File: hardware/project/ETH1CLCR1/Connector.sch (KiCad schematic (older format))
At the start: 1 part, among them J1101 C64AC

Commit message: Schematic design
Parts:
- added C1621, C1622, C1623, C1624, C1625, C1626: 10p, Capacitor_SMD:C_0603_1608Metric_Pad1.05x0.95mm_HandSolder, symbol Device:C
- added K1001, K1002, K1003, K1004, K1005, K1006: HE3621A0510, symbol ETH1CLCR1:HE3621A0510
- added Q1605, Q1606, Q1607, Q1608, Q1609, Q1610: BC847W, Package_TO_SOT_SMD:SOT-323_SC-70, symbol Transistor_BJT:BC847W
- added R1621, R1622, R1623, R1624, R1625, R1626: 10k, Resistor_SMD:R_0603_1608Metric_Pad1.05x0.95mm_HandSolder, symbol Device:R
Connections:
- net A: now also K1001.4
- net B: now also K1002.4
- net C: now also K1003.4
- net D: now also K1004.4
- net E: now also K1005.4
- net F: now also K1006.4
- new net: K1001.3, Q1605.3 (C)
- new net: K1002.3, Q1606.3 (C)
- new net: K1003.3, Q1607.3 (C)
- new net: K1004.3, Q1608.3 (C)
- new net: K1005.3, Q1609.3 (C)
- new net: K1006.3, Q1610.3 (C)
- new net: C1621.1, Q1605.1 (B), R1621.2
- new net: C1622.1, Q1606.1 (B), R1622.2
- new net: C1623.1, Q1607.1 (B), R1623.2
- new net: C1624.1, Q1608.1 (B), R1624.2
- new net: C1625.1, Q1609.1 (B), R1625.2
- new net: C1626.1, Q1610.1 (B), R1626.2
- new net +5VF: K1001.2, K1002.2, K1003.2, K1004.2, K1005.2, K1006.2
- new net AGNDF: C1621.2, C1622.2, C1623.2, C1624.2, C1625.2, C1626.2, K1004.1, Q1605.2 (E), Q1606.2 (E), Q1607.2 (E), Q1608.2 (E), Q1609.2 (E), Q1610.2 (E)
- new net CXN_RELA: R1621.1
- new net CXN_RELB: R1622.1
- new net CXN_RELC: R1623.1
- new net CXN_RELD: R1624.1
- new net CXN_RELE: R1625.1
- new net CXN_RELF: R1626.1
- new net GUARD: K1003.1
- new net HCUR: K1001.1
- new net HPOT: K1006.1
- new net LCUR: K1002.1
- new net LPOT: K1005.1

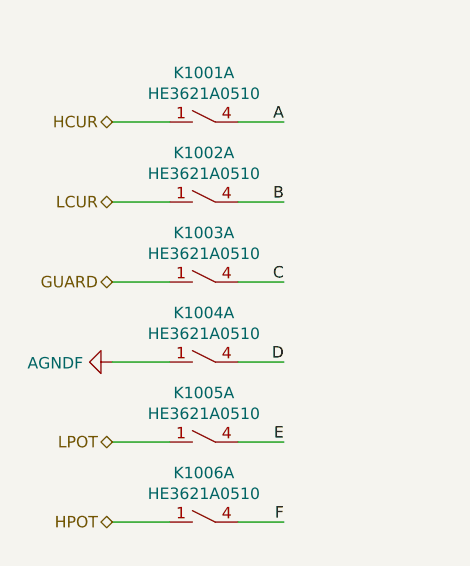
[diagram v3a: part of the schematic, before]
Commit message: Need to redesign the AC source, the LT1468 is too slow.
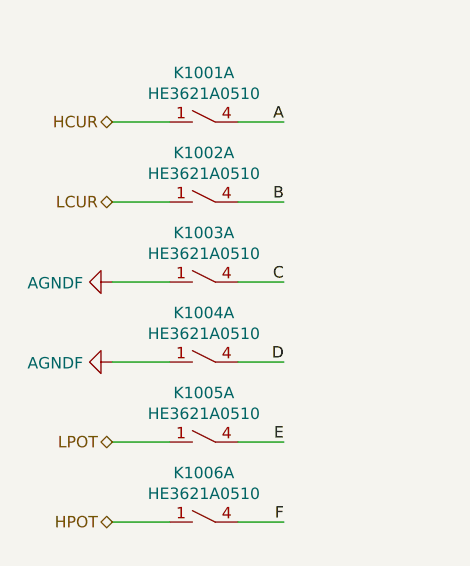
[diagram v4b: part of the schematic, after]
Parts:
- K1001, K1002, K1003, K1004, K1005, K1006: footprint (none) -> ETH1CLCR1:HE360_x-5050462-8
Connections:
- net GUARD is gone; now on net AGNDF: K1003.1
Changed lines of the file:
@@
 F 0 "K1001" V 3865 1300 50  0000 C CNN
 F 1 "HE3621A0510" V 3774 1300 50  0000 C CNN
-F 2 "" H 3900 1250 50  0001 C CNN
+F 2 "ETH1CLCR1:HE360_x-5050462-8" H 3900 1250 50  0001 C CNN
 F 3 "" H 3900 1250 50  0001 C CNN
 	1    3650 1300
@@
 F 0 "K1001" H 7978 1946 50  0000 L CNN
 F 1 "HE3621A0510" H 7978 1855 50  0000 L CNN
-F 2 "" H 8150 1850 50  0001 C CNN
+F 2 "ETH1CLCR1:HE360_x-5050462-8" H 8150 1850 50  0001 C CNN
 F 3 "" H 8150 1850 50  0001 C CNN
 	2    7900 1900
@@
 F 0 "K1002" V 3865 1650 50  0000 C CNN
 F 1 "HE3621A0510" V 3774 1650 50  0000 C CNN
-F 2 "" H 3900 1600 50  0001 C CNN
+F 2 "ETH1CLCR1:HE360_x-5050462-8" H 3900 1600 50  0001 C CNN
 F 3 "" H 3900 1600 50  0001 C CNN
 	1    3650 1650
@@
 F 0 "K1002" H 9728 1946 50  0000 L CNN
 F 1 "HE3621A0510" H 9728 1855 50  0000 L CNN
-F 2 "" H 9900 1850 50  0001 C CNN
+F 2 "ETH1CLCR1:HE360_x-5050462-8" H 9900 1850 50  0001 C CNN
 F 3 "" H 9900 1850 50  0001 C CNN
 	2    9650 1900
@@
 F 0 "K1003" V 3865 2000 50  0000 C CNN
 F 1 "HE3621A0510" V 3774 2000 50  0000 C CNN
-F 2 "" H 3900 1950 50  0001 C CNN
+F 2 "ETH1CLCR1:HE360_x-5050462-8" H 3900 1950 50  0001 C CNN
 F 3 "" H 3900 1950 50  0001 C CNN
 	1    3650 2000
@@
 F 0 "K1003" H 7978 3446 50  0000 L CNN
 F 1 "HE3621A0510" H 7978 3355 50  0000 L CNN
-F 2 "" H 8150 3350 50  0001 C CNN
+F 2 "ETH1CLCR1:HE360_x-5050462-8" H 8150 3350 50  0001 C CNN
 F 3 "" H 8150 3350 50  0001 C CNN
 	2    7900 3400
@@
 F 0 "K1004" V 3865 2350 50  0000 C CNN
 F 1 "HE3621A0510" V 3774 2350 50  0000 C CNN
-F 2 "" H 3900 2300 50  0001 C CNN
+F 2 "ETH1CLCR1:HE360_x-5050462-8" H 3900 2300 50  0001 C CNN
 F 3 "" H 3900 2300 50  0001 C CNN
 	1    3650 2350
@@
 F 0 "K1004" H 9728 3446 50  0000 L CNN
 F 1 "HE3621A0510" H 9728 3355 50  0000 L CNN
-F 2 "" H 9900 3350 50  0001 C CNN
+F 2 "ETH1CLCR1:HE360_x-5050462-8" H 9900 3350 50  0001 C CNN
 F 3 "" H 9900 3350 50  0001 C CNN
 	2    9650 3400
@@
 F 0 "K1005" V 3865 2700 50  0000 C CNN
 F 1 "HE3621A0510" V 3774 2700 50  0000 C CNN
-F 2 "" H 3900 2650 50  0001 C CNN
+F 2 "ETH1CLCR1:HE360_x-5050462-8" H 3900 2650 50  0001 C CNN
 F 3 "" H 3900 2650 50  0001 C CNN
 	1    3650 2700
@@
 F 0 "K1005" H 7978 4996 50  0000 L CNN
 F 1 "HE3621A0510" H 7978 4905 50  0000 L CNN
-F 2 "" H 8150 4900 50  0001 C CNN
+F 2 "ETH1CLCR1:HE360_x-5050462-8" H 8150 4900 50  0001 C CNN
 F 3 "" H 8150 4900 50  0001 C CNN
 	2    7900 4950
@@
 F 0 "K1006" V 3865 3050 50  0000 C CNN
 F 1 "HE3621A0510" V 3774 3050 50  0000 C CNN
-F 2 "" H 3900 3000 50  0001 C CNN
+F 2 "ETH1CLCR1:HE360_x-5050462-8" H 3900 3000 50  0001 C CNN
 F 3 "" H 3900 3000 50  0001 C CNN
 	1    3650 3050
@@
 F 0 "K1006" H 9728 4996 50  0000 L CNN
 F 1 "HE3621A0510" H 9728 4905 50  0000 L CNN
-F 2 "" H 9900 4900 50  0001 C CNN
+F 2 "ETH1CLCR1:HE360_x-5050462-8" H 9900 4900 50  0001 C CNN
 F 3 "" H 9900 4900 50  0001 C CNN
 	2    9650 4950
@@
 Text HLabel 3250 2700 0    50   BiDi ~ 0
 LPOT
-Text HLabel 3250 2000 0    50   BiDi ~ 0
-GUARD
 $Comp
 L Transistor_BJT:BC847W Q1605
@@
 	0    1    1    0
 $EndComp
+$Comp
+L ETH1CLCR1:AGNDF #PWR01650
+U 1 1 5E2C2319
+P 3250 2000
+F 0 "#PWR01650" H 3250 1750 50  0001 C CNN
+F 1 "AGNDF" V 3255 1872 50  0000 R CNN
+F 2 "" H 3250 2000 50  0001 C CNN
+F 3 "" H 3250 2000 50  0001 C CNN
+	1    3250 2000
+	0    1    1    0
+$EndComp

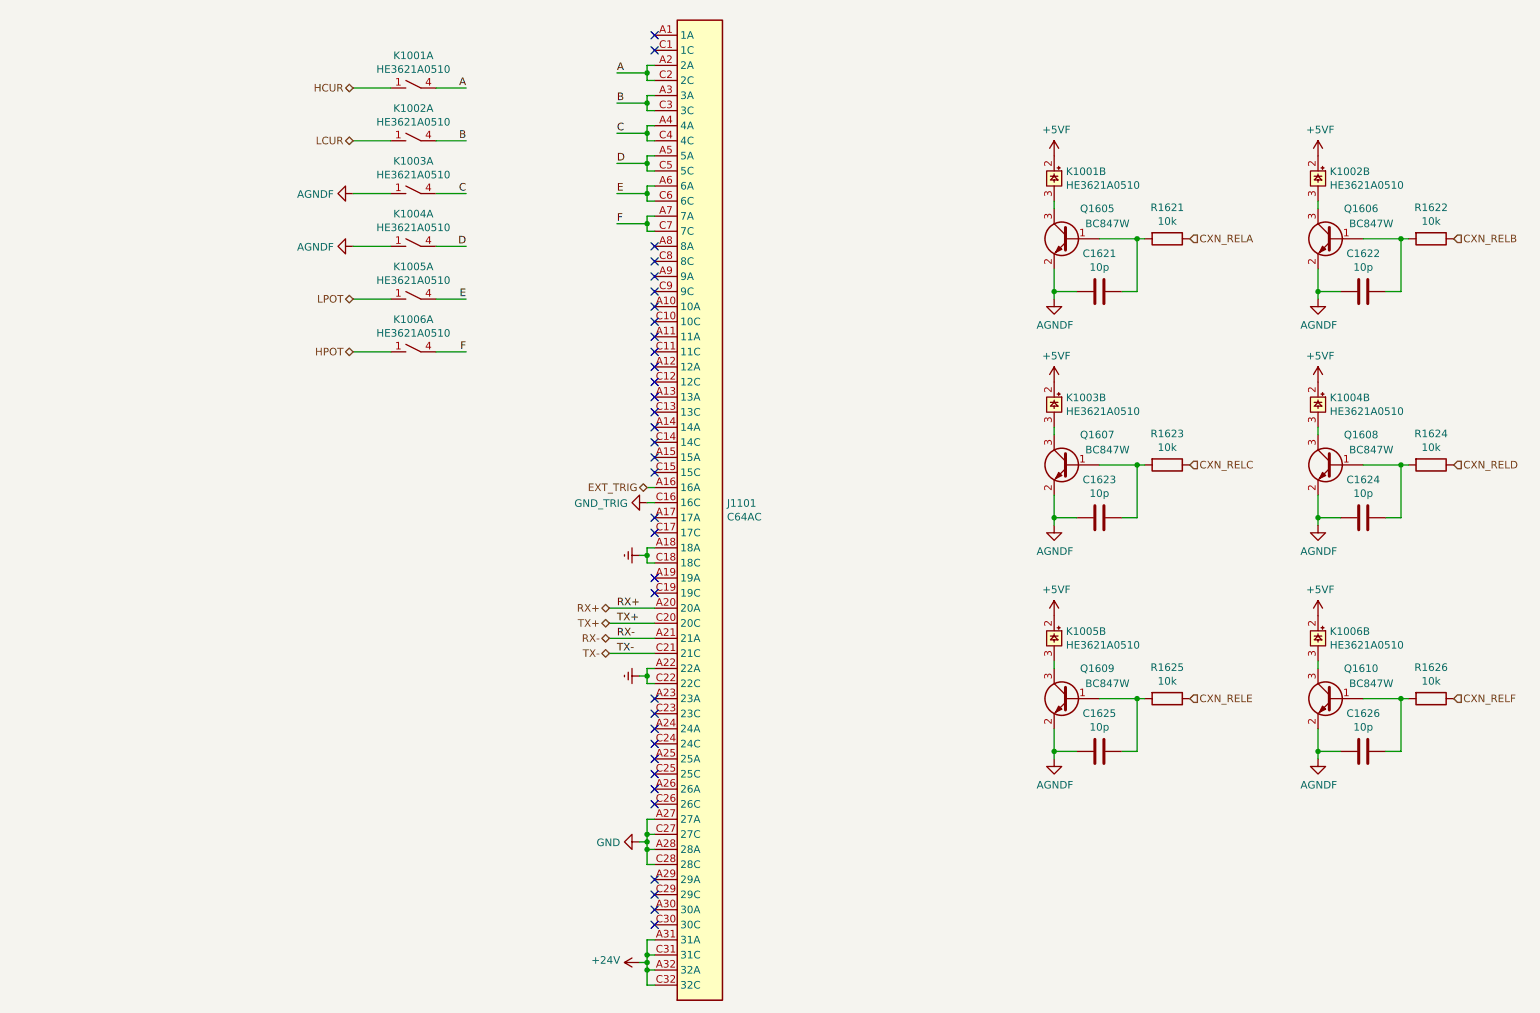
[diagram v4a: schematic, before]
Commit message: Footprint asigment (not finished).
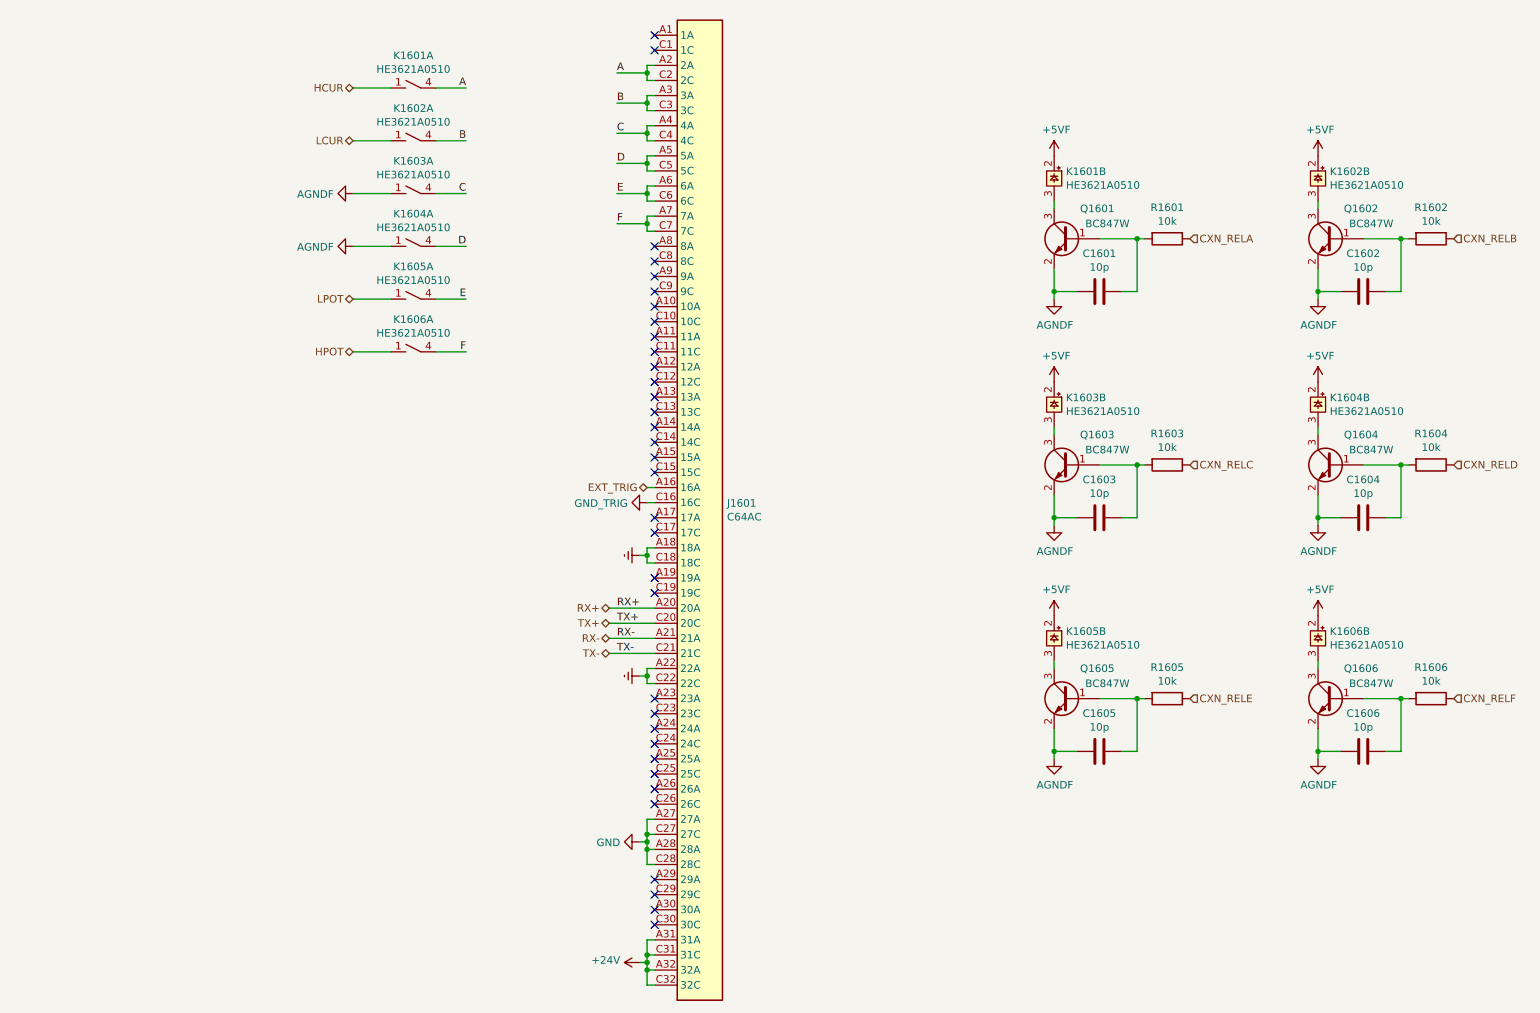
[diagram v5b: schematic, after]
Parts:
- renumbered C1621 to C1601, C1622 to C1602, C1623 to C1603, C1624 to C1604, C1625 to C1605, C1626 to C1606, J1101 to J1601, K1001 to K1601, K1002 to K1602, K1003 to K1603, K1004 to K1604, K1005 to K1605, K1006 to K1606, Q1605 to Q1601, Q1606 to Q1602, Q1607 to Q1603, Q1608 to Q1604, Q1609 to Q1605, Q1610 to Q1606, R1621 to R1601, R1622 to R1602, R1623 to R1603, R1624 to R1604, R1625 to R1605, R1626 to R1606

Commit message: Modification in schematic and PCB layout.
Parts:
- removed C1601, C1602, C1603, C1604, C1605, C1606: 10p, Capacitor_SMD:C_0603_1608Metric_Pad1.05x0.95mm_HandSolder, symbol Device:C
- removed Q1601, Q1602, Q1603, Q1604, Q1605, Q1606: BC847W, Package_TO_SOT_SMD:SOT-323_SC-70, symbol Transistor_BJT:BC847W
- removed R1601, R1602, R1603, R1604, R1605, R1606: 10k, Resistor_SMD:R_0603_1608Metric_Pad1.05x0.95mm_HandSolder, symbol Device:R
- added U1601: ULN2003A, Package_SO:TSSOP-16_4.4x5mm_P0.65mm, symbol Transistor_Array:ULN2003A
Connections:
- net +5VF: now also U1601.9 (COM)
- net AGNDF: now also U1601.8 (GND)
- net at K1601.3: now also U1601.16 (O1)
- net at K1602.3: now also U1601.15 (O2)
- net at K1603.3: now also U1601.14 (O3)
- net at K1604.3: now also U1601.13 (O4)
- net at K1605.3: now also U1601.12 (O5)
- net at K1606.3: now also U1601.11 (O6)
- new net CXN_REL1: U1601.1 (I1)
- new net CXN_REL2: U1601.2 (I2)
- new net CXN_REL3: U1601.3 (I3)
- new net CXN_REL4: U1601.4 (I4)
- new net CXN_REL5: U1601.5 (I5)
- new net CXN_REL6: U1601.6 (I6)
- no-connect marks 34 -> 36
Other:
- moved on the sheet: J1601
